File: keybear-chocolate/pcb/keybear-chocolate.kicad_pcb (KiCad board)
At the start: 2 copper layers, 136.9 x 98.2 mm, 103 parts, among them J1 MJ-4PP-9, J2 BATT, J3 LED, J4 OLED, P1 USB_C_Plug, SW1 SW_PUSH, SW10 SW_PUSH, SW11 SW_PUSH, SW12 SW_PUSH, SW13 SW_PUSH, SW14 SW_PUSH, SW15 SW_PUSH, SW16 SW_PUSH, SW17 SW_PUSH, SW18 SW_PUSH, SW19 SW_PUSH, SW2 SW_PUSH, SW20 SW_PUSH, SW21 SW_PUSH, SW22 SW_PUSH, SW24 Rotary_Encoder_Switch, SW3 SW_PUSH, SW30 BATT_SW, SW4 SW_PUSH, SW5 SW_PUSH, SW6 SW_PUSH, SW7 SW_PUSH, SW8 SW_PUSH, SW9 SW_PUSH, U1 ProMicro

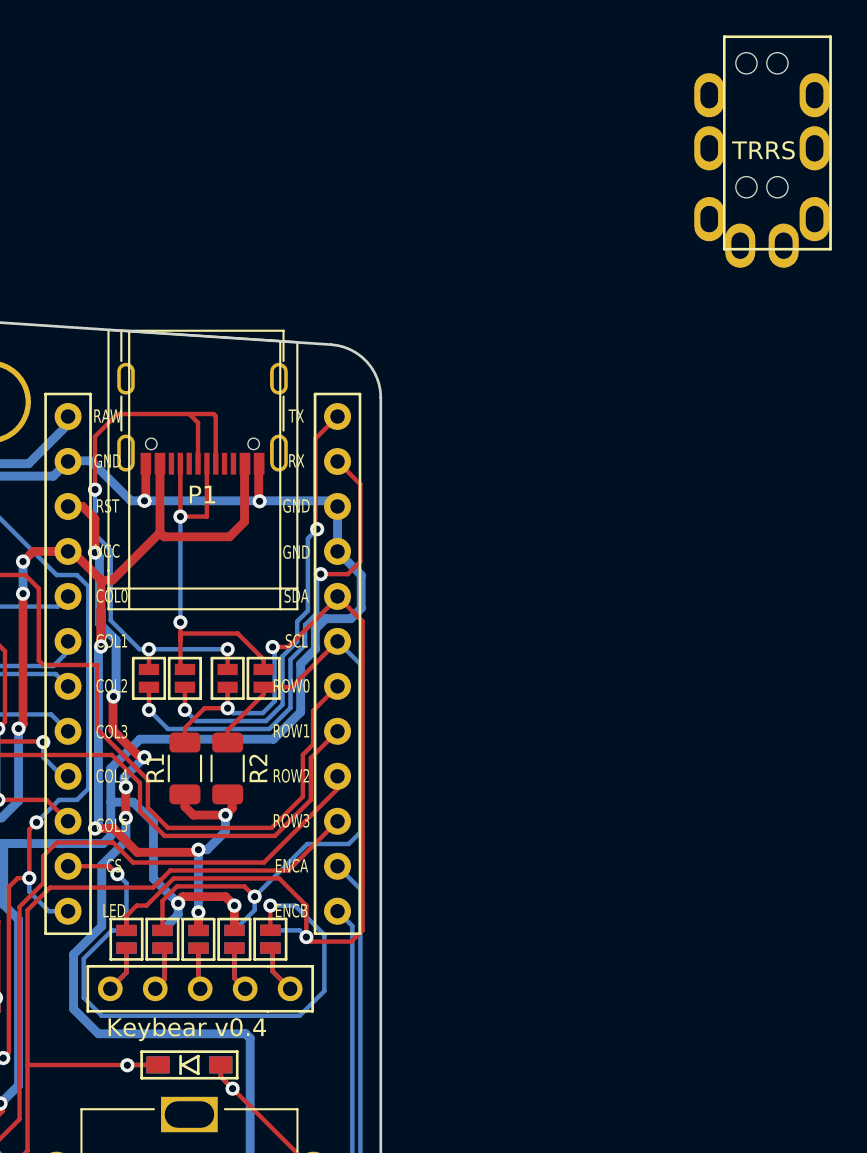
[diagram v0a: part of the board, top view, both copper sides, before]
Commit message: trrs deleted. usb-c connected - v0.5
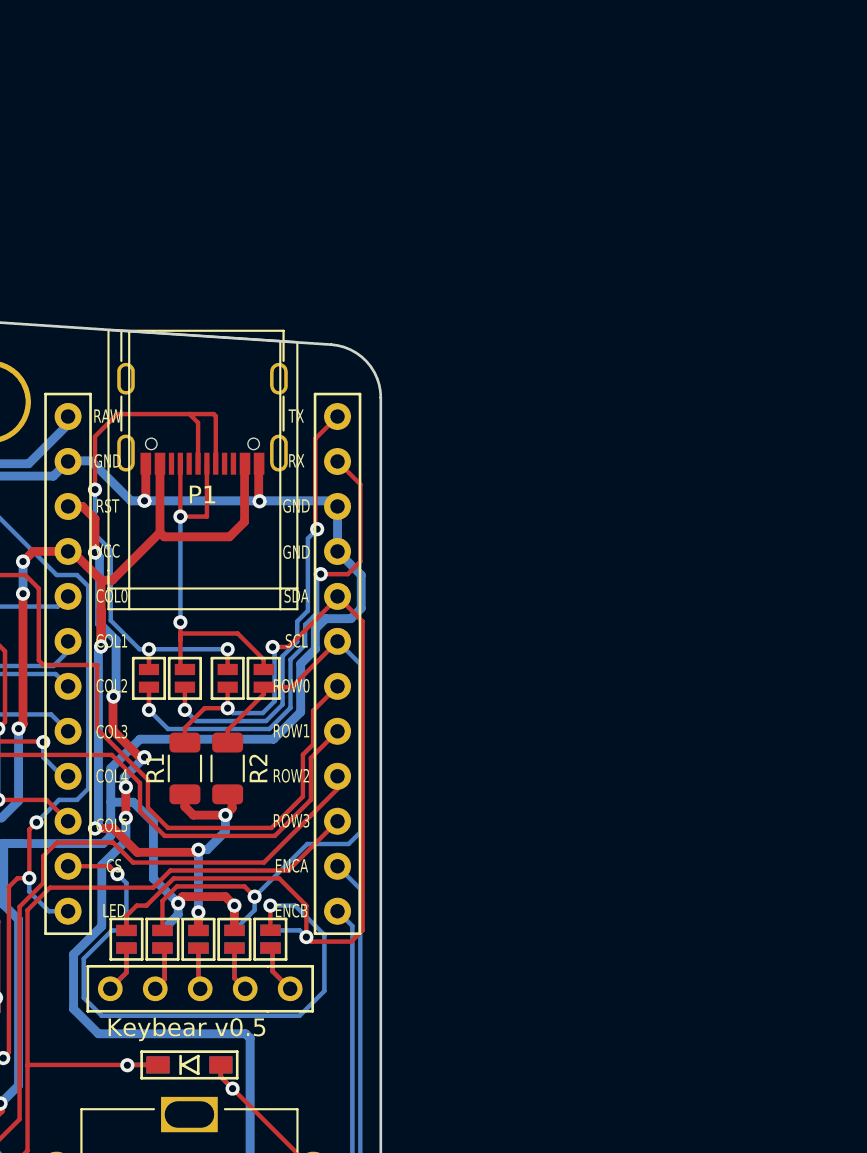
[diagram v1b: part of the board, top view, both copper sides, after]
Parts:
- removed J1: MJ-4PP-9, kbd:MJ-4PP-9
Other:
- board text added: "Keybear v0.5"
- board text removed: "Keybear v0.4"

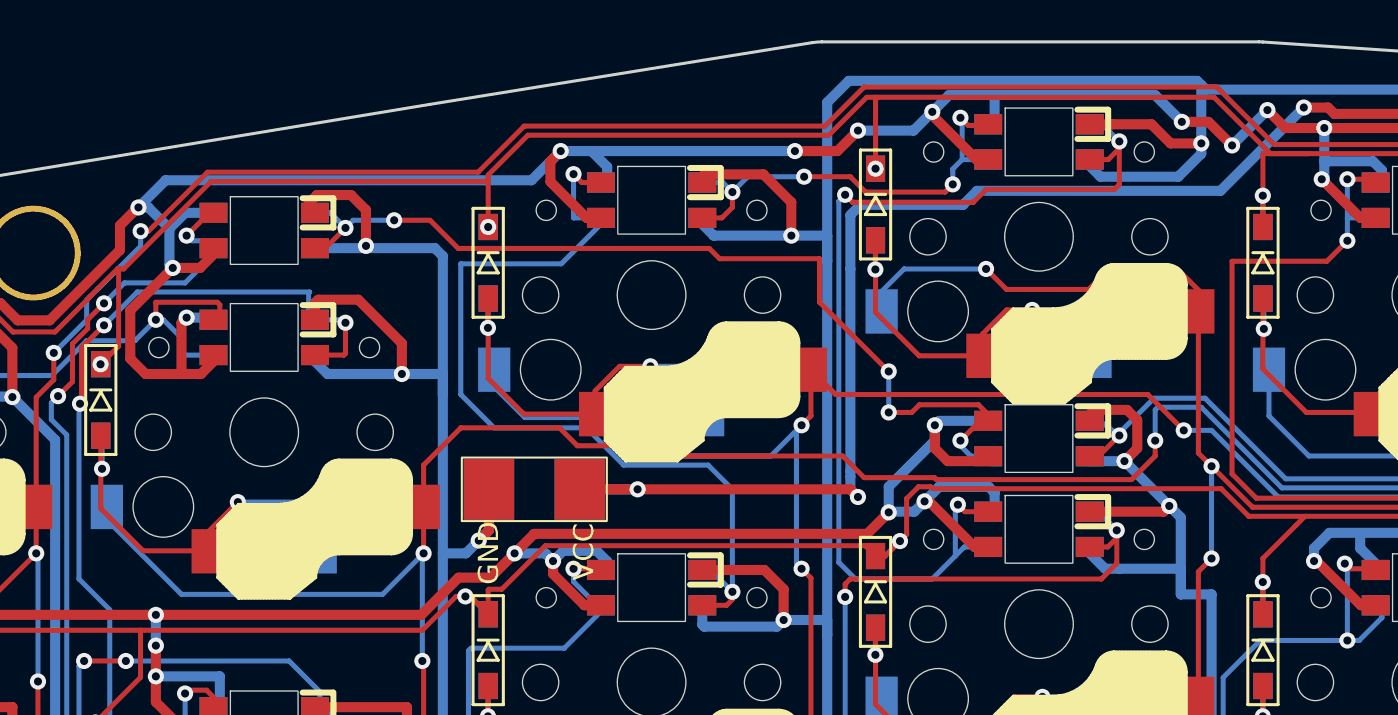
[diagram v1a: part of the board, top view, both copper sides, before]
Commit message: making space at the top left to add exteranl GPIO pins
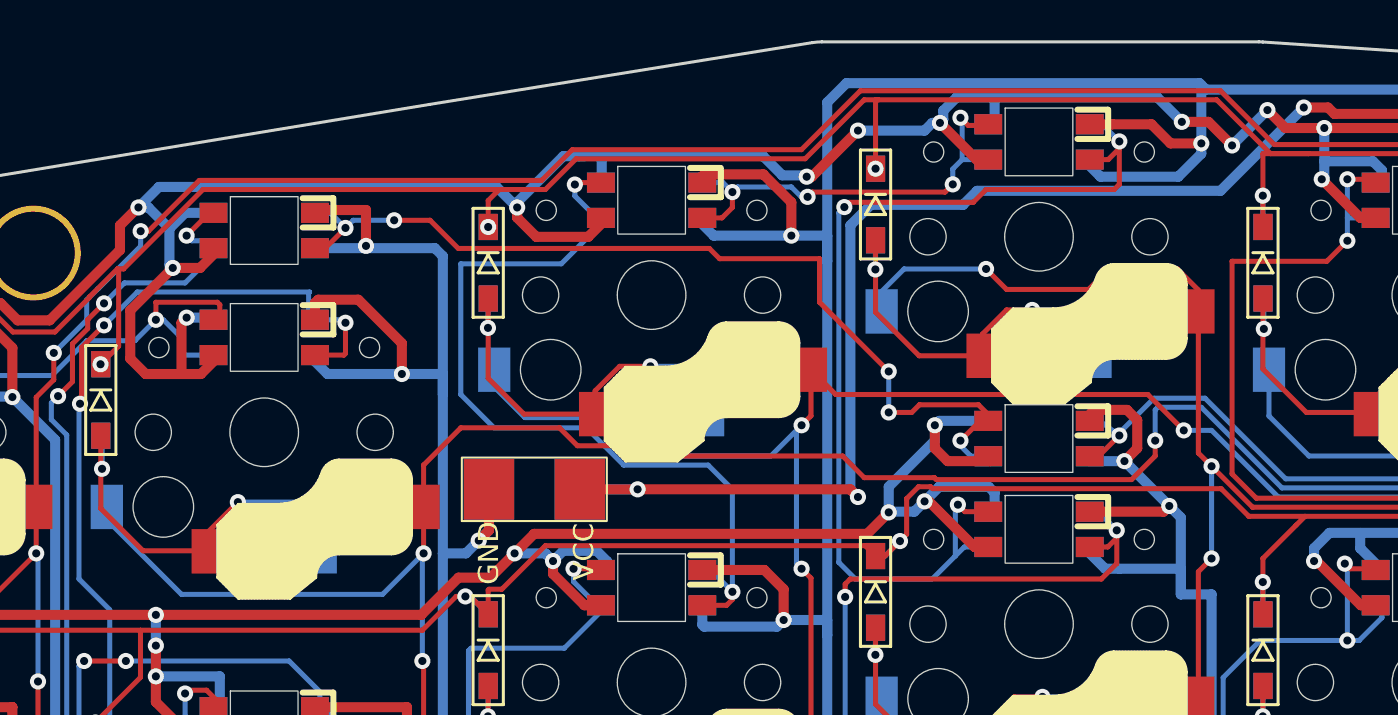
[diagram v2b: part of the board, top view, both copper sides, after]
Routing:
- net VCC: track 891.8 -> 893.3 mm
- net Net-(L3-DOUT): track 45.8 -> 44.4 mm
- net GND: track 910.2 -> 909.3 mm
- net Net-(L10-DOUT): track 52.6 -> 52.0 mm
- net row0: track 190.1 -> 189.5 mm

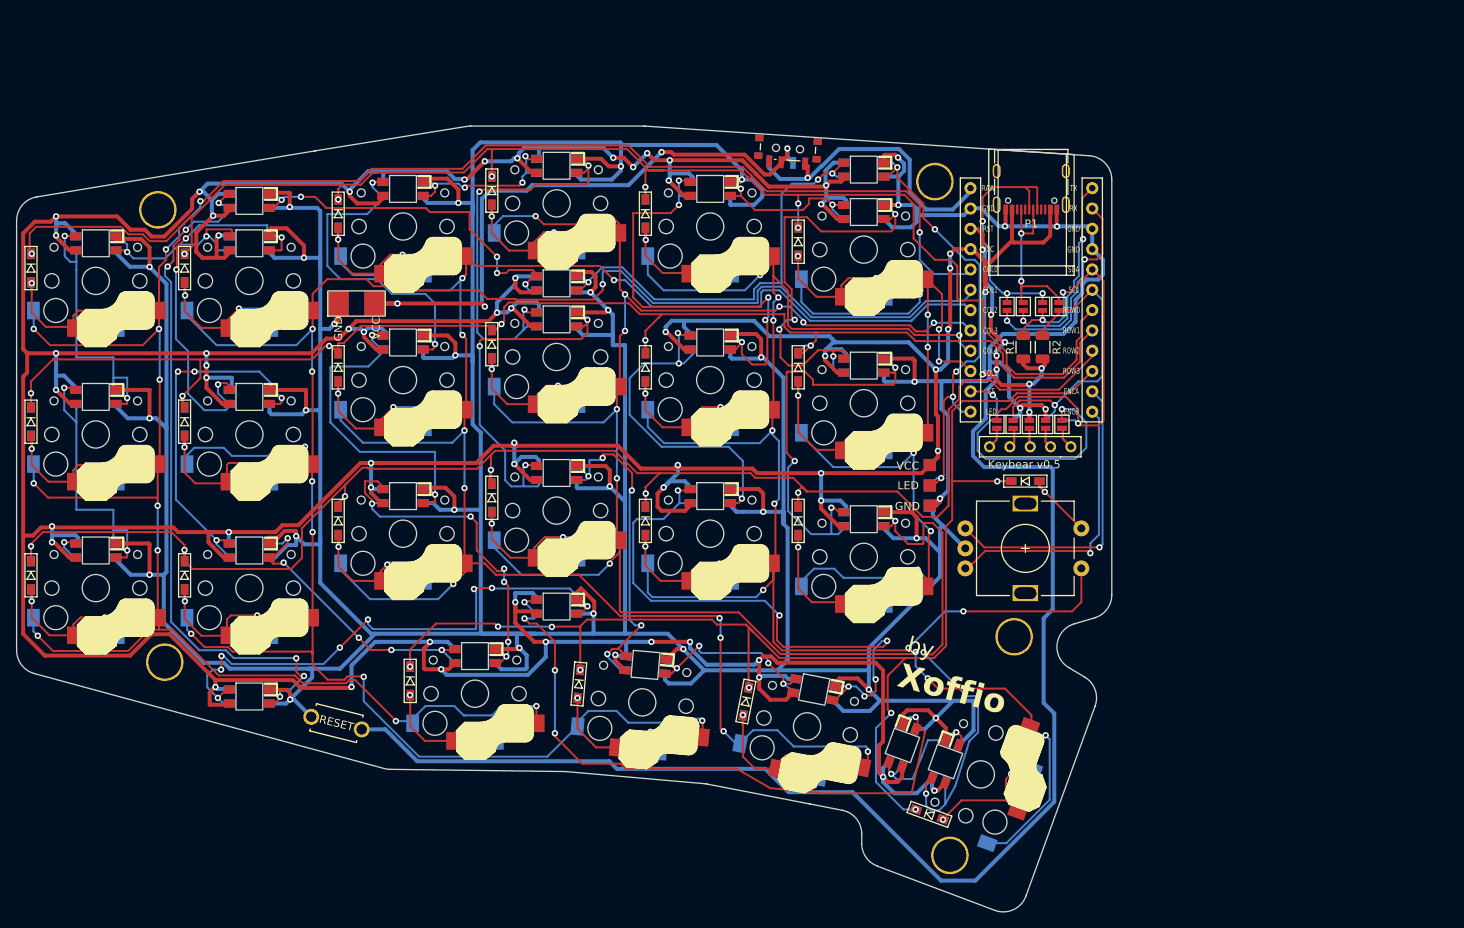
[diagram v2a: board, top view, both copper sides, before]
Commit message: connecting MPC23P17_ML
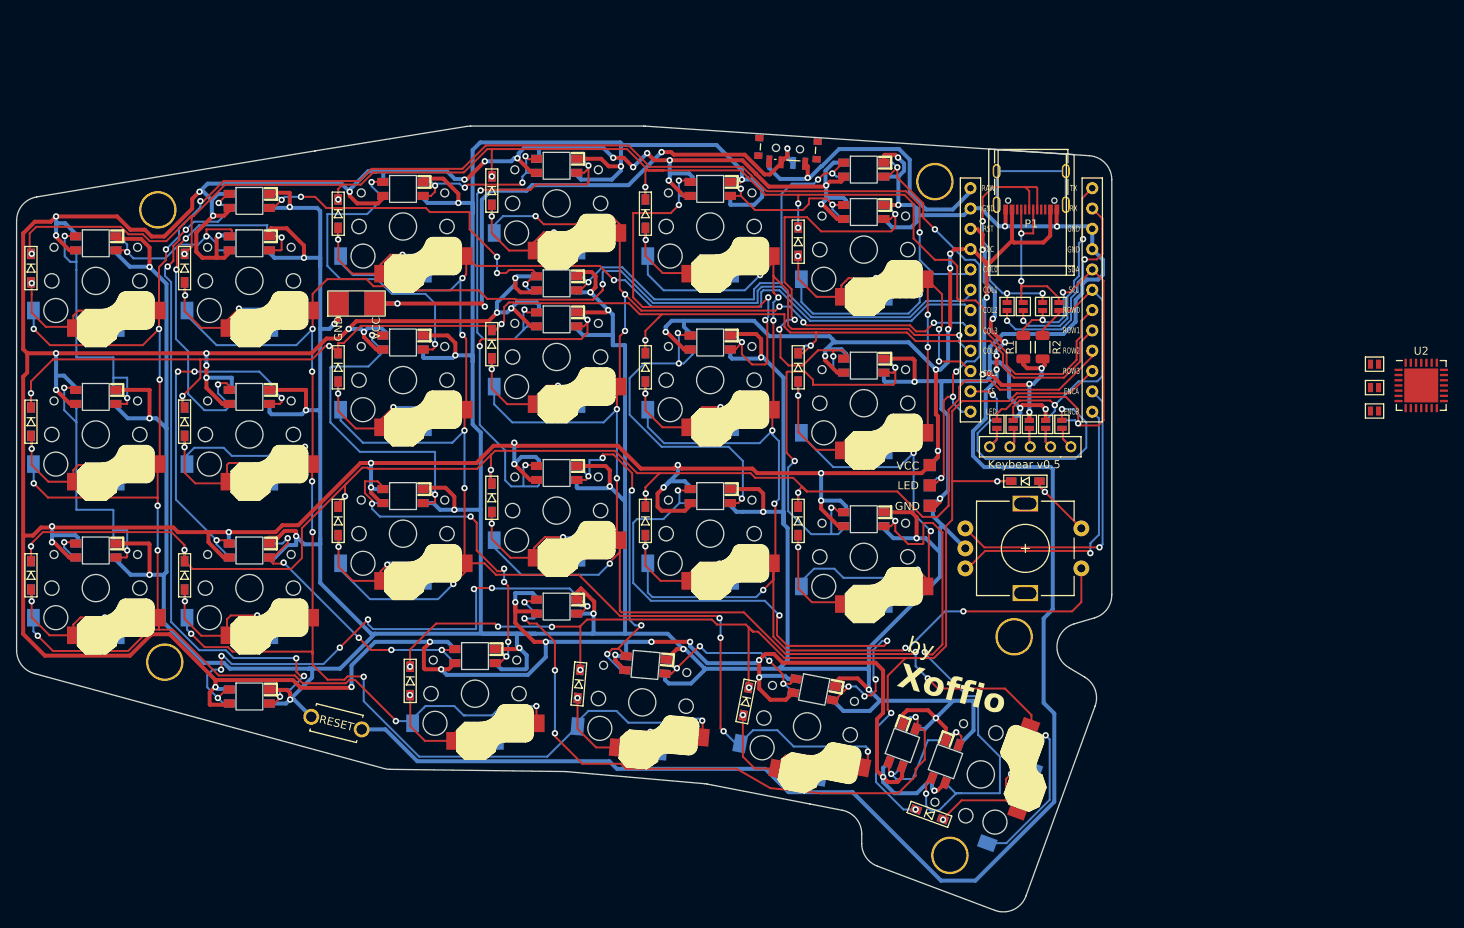
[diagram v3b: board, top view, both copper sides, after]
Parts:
- added JP16: , kbd:Jumper, F.Cu at (309.8, 122.0)
- added JP17: , kbd:Jumper, F.Cu at (309.8, 124.9)
- added JP18: , kbd:Jumper, F.Cu at (309.8, 127.9)
- added U2: MCP23017_ML, Package_DFN_QFN:QFN-28-1EP_6x6mm_P0.65mm_EP4.25x4.25mm, F.Cu at (315.7, 124.7)
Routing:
- net unconnected-(P1-SHIELD-PadS1): track 0.00 -> 17.0 mm
- net Net-(L18-DIN): track 65.2 -> 71.0 mm
- net VCC: track 893.3 -> 891.5 mm
- net row0: track 189.5 -> 188.9 mm

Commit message: adding ATECC608A-SSHDA crypto chip
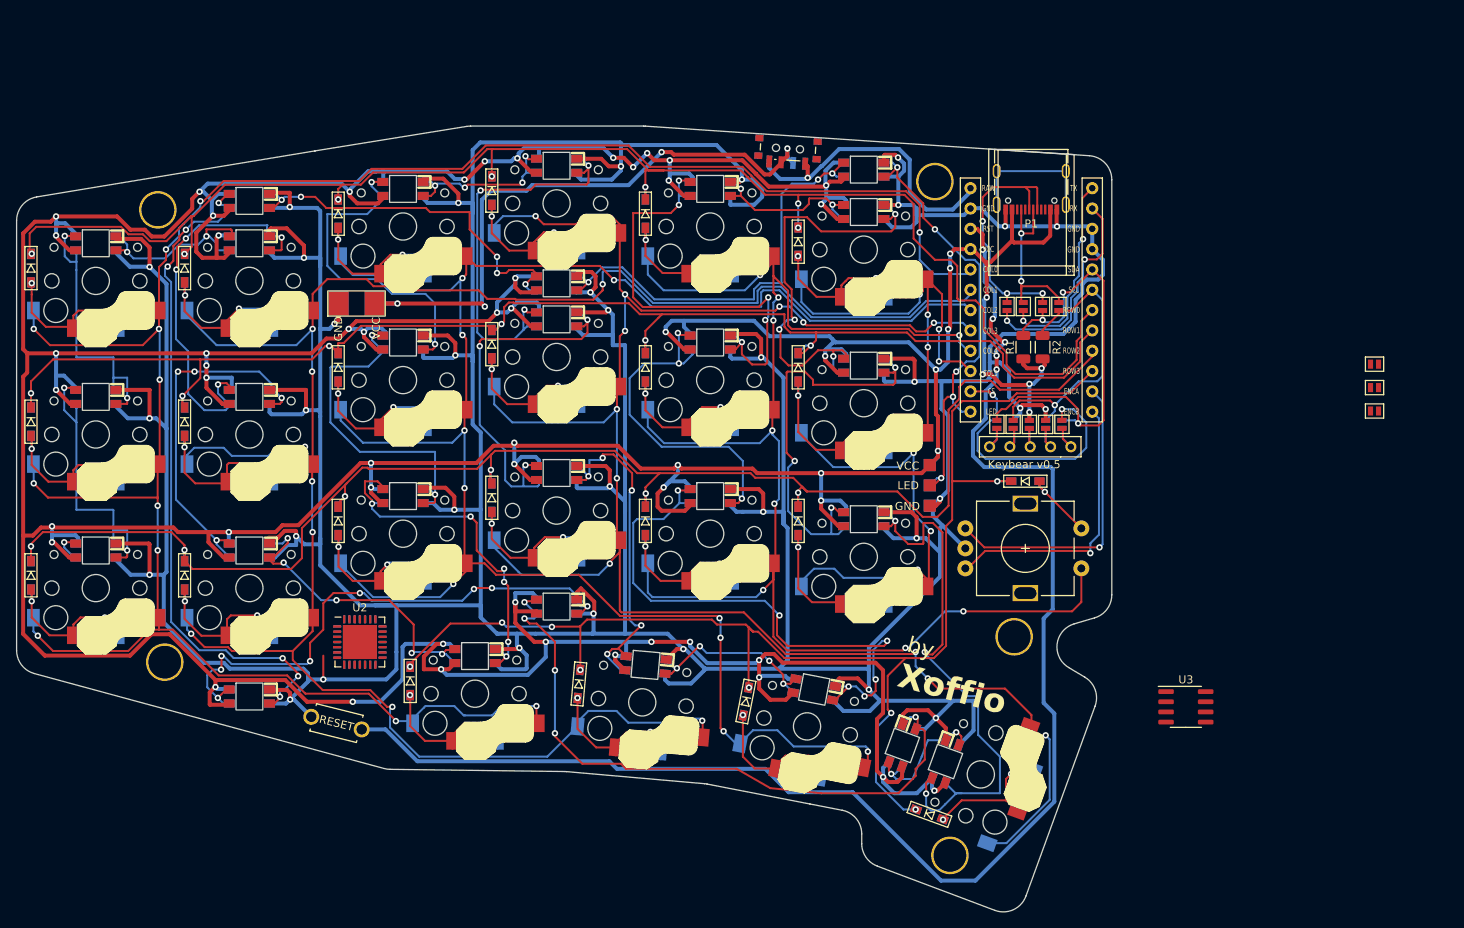
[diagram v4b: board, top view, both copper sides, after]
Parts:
- added U2: MCP23017_ML, Package_DFN_QFN:QFN-28-1EP_6x6mm_P0.65mm_EP4.25x4.25mm, B.Cu at (183.0, 156.7)
- added U3: ATECC608A-SSHDA, Package_SO:SOIC-8_3.9x4.9mm_P1.27mm, F.Cu at (286.3, 164.8)
- moved U2 136.5 mm to (183.0, 156.7)
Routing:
- net GND: track 909.0 -> 914.6 mm, vias 33 -> 34
- net VCC: track 891.5 -> 894.5 mm
- net Net-(L14-DIN): track 38.1 -> 40.8 mm
- net Net-(L27-DIN): track 89.5 -> 87.3 mm
- net row3: track 169.6 -> 168.7 mm
- net Net-(L26-DIN): track 70.5 -> 69.9 mm
- net col2: track 238.4 -> 237.8 mm
